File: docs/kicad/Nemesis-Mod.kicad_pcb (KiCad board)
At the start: 2 copper layers, 45.7 x 59.7 mm, 7 parts, among them P1 Power, SW1 Reset

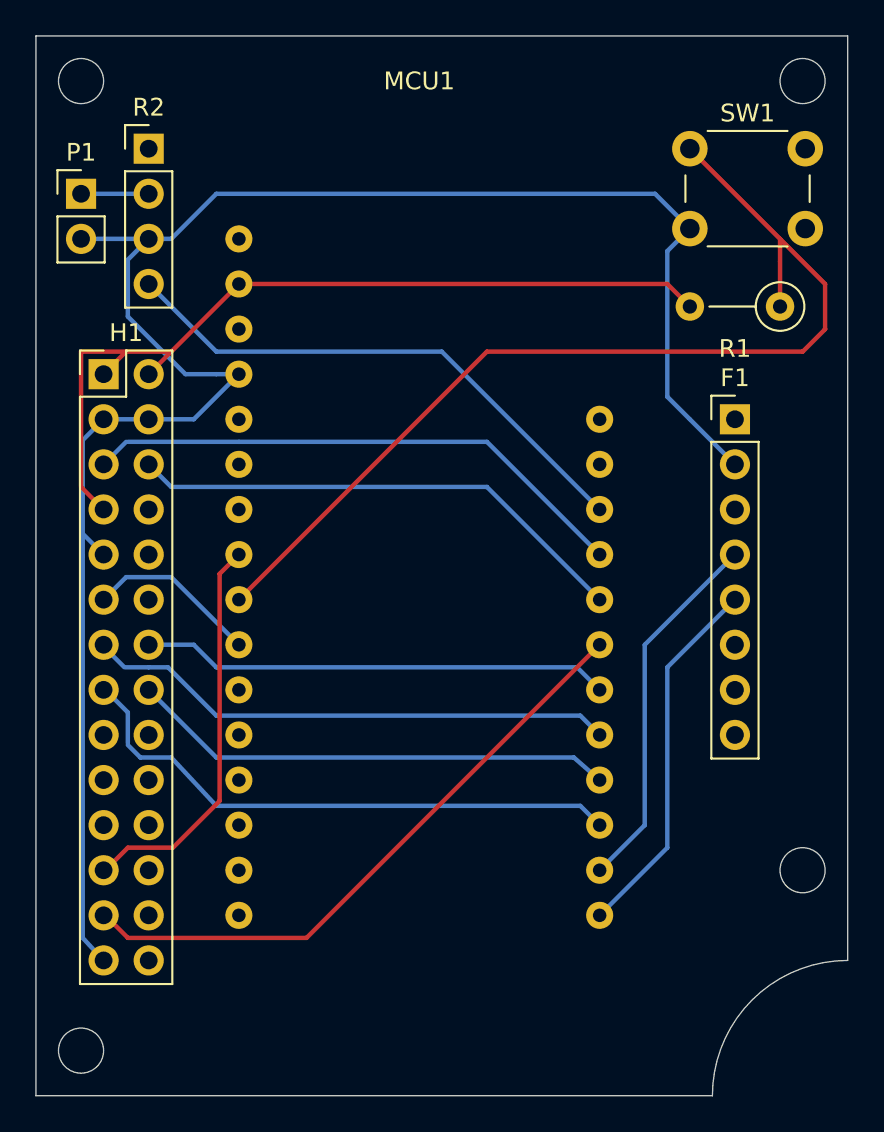
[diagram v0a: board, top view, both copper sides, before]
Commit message: Fixing schematic issues after double checking before fabrication.
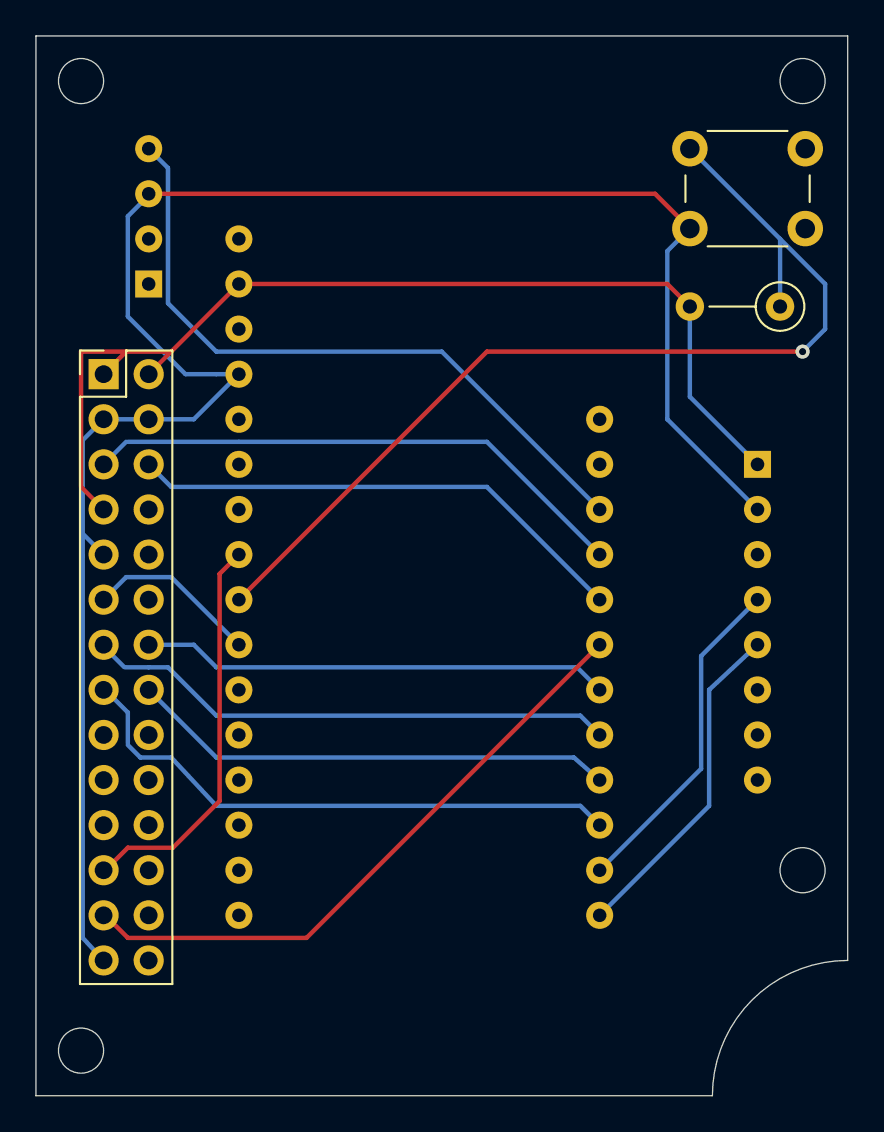
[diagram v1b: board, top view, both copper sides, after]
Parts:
- removed R2: 5V Regulator, Connector_PinHeader_2.54mm:PinHeader_1x04_P2.54mm_Vertical
- F1: footprint Connector_PinHeader_2.54mm:PinHeader_1x08_P2.54mm_Vertical -> Adafruit:Adafruit_I2C_FRAM_Breakout; moved to B.Cu
- P1: value Power -> Pololu_5V_Step_Down_Regulator; footprint Connector_PinHeader_2.54mm:PinHeader_1x02_P2.54mm_Vertical -> Pololu:5V_Step_Down_Regulator_500mA; moved to B.Cu
- moved F1 12.0 mm to (124.5, 110.5), turned to 270 degrees
- moved P1 8.98 mm to (100.3, 87.6), turned to 90 degrees
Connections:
- P1 pad 1: 11V -> Net-(P1-Pad1)
- P1 pad 2: GND -> 11V
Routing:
- net 3V: track 49.4 -> 59.9 mm
- net 5V: track 30.7 -> 38.3 mm
- net 11V: track 3.81 -> 0.00 mm
- net SCL: track 20.9 -> 18.9 mm
- net SDA: track 20.9 -> 19.0 mm
- net GND: track 105.6 -> 106.3 mm
- net /RESET_DOWN: vias 0 -> 1

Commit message: Upgrading KiCad project to v6.
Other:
- net class Default removed

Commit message: Updating PCB to match schematic.
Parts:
- SW1: value Reset -> SW1
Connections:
- net /BT_INT renamed /Mainboard/BT_INT
- net /FIRE_DOWN renamed /Mainboard/FIRE_DOWN
- net /M1PWM renamed /Mainboard/M1PWM
- net /M1SLP renamed /Mainboard/M1SLP
- net /M2PWM renamed /Mainboard/M2PWM
- net /M2SLP renamed /Mainboard/M2SLP
- net /M3PWM renamed /Mainboard/M3PWM
- net /M3SLP renamed /Mainboard/M3SLP
- net /RESET_DOWN renamed /Mainboard/RESET_DOWN
- net /REV_DOWN renamed /Mainboard/REV_DOWN
- net /SOFT_LOCK1 renamed /Hopper Lock/SOFT_LOCK1
- net 11V renamed /Flywheels/V_{BATT}
- net 3V renamed +3V3
- net 5V renamed +5V
- net SCL renamed /Mainboard/SCL
- net SDA renamed /Mainboard/SDA
- F1 pad 3: Net-(F1-Pad3) -> unconnected-(F1-Pad3)
- F1 pad 6: Net-(F1-Pad6) -> unconnected-(F1-Pad6)
- F1 pad 7: Net-(F1-Pad7) -> unconnected-(F1-Pad7)
- F1 pad 8: Net-(F1-Pad8) -> unconnected-(F1-Pad8)
- H1 pad 10: Net-(H1-Pad10) -> unconnected-(H1-Pad10)
- H1 pad 12: Net-(H1-Pad12) -> unconnected-(H1-Pad12)
- H1 pad 17: Net-(H1-Pad17) -> unconnected-(H1-Pad17)
- H1 pad 18: Net-(H1-Pad18) -> unconnected-(H1-Pad18)
- H1 pad 19: Net-(H1-Pad19) -> unconnected-(H1-Pad19)
- H1 pad 20: Net-(H1-Pad20) -> unconnected-(H1-Pad20)
- H1 pad 21: Net-(H1-Pad21) -> unconnected-(H1-Pad21)
- H1 pad 22: Net-(H1-Pad22) -> unconnected-(H1-Pad22)
- H1 pad 24: Net-(H1-Pad24) -> unconnected-(H1-Pad24)
- H1 pad 26: Net-(H1-Pad26) -> unconnected-(H1-Pad26)
- H1 pad 28: Net-(H1-Pad28) -> unconnected-(H1-Pad28)
- H1 pad 8: Net-(H1-Pad8) -> unconnected-(H1-Pad8)
- MCU1 pad 1: Net-(MCU1-Pad1) -> unconnected-(MCU1-Pad1)
- MCU1 pad 11: Net-(MCU1-Pad11) -> unconnected-(MCU1-Pad11)
- MCU1 pad 12: Net-(MCU1-Pad12) -> unconnected-(MCU1-Pad12)
- MCU1 pad 13: Net-(MCU1-Pad13) -> unconnected-(MCU1-Pad13)
- MCU1 pad 14: Net-(MCU1-Pad14) -> unconnected-(MCU1-Pad14)
- MCU1 pad 15: Net-(MCU1-Pad15) -> unconnected-(MCU1-Pad15)
- MCU1 pad 16: Net-(MCU1-Pad16) -> unconnected-(MCU1-Pad16)
- MCU1 pad 17: Net-(MCU1-Pad17) -> unconnected-(MCU1-Pad17)
- MCU1 pad 18: Net-(MCU1-Pad18) -> unconnected-(MCU1-Pad18)
- MCU1 pad 3: Net-(MCU1-Pad3) -> unconnected-(MCU1-Pad3)
- MCU1 pad 6: Net-(MCU1-Pad6) -> unconnected-(MCU1-Pad6)
- MCU1 pad 7: Net-(MCU1-Pad7) -> unconnected-(MCU1-Pad7)
- P1 pad 1: Net-(P1-Pad1) -> unconnected-(P1-Pad1)
